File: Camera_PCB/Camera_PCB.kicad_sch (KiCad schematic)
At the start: 1 part, among them U1 V3s-eLQFP128

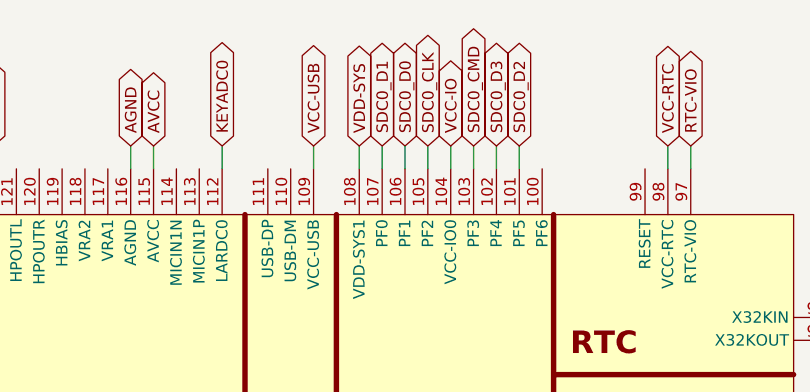
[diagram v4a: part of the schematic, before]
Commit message: Readded Camera, USB connections
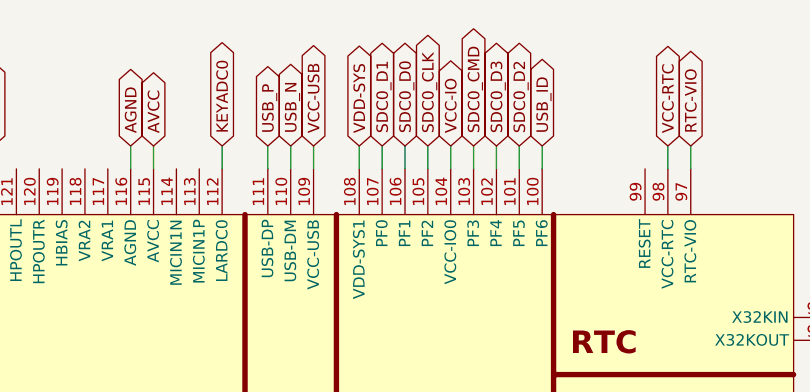
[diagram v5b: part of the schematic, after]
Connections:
- net USB_ID: now reaches U1.100 (PF6)
- net USB_N: now reaches U1.110 (USB-DM)
- net USB_P: now reaches U1.111 (USB-DP)
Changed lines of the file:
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@@
+	(wire
+		(pts
+			(xy 109.22 26.67) (xy 109.22 29.21)
+		)
+		(stroke
+			(width 0)
+			(type default)
+		)
+	)
 	(wire
 		(pts
@@
 	(wire
 		(pts
+			(xy 106.68 26.67) (xy 106.68 29.21)
+		)
+		(stroke
+			(width 0)
+			(type default)
+		)
+	)
+	(wire
+		(pts
 			(xy 170.18 95.25) (xy 172.72 95.25)
 		)
@@
 	(wire
 		(pts
+			(xy 137.16 26.67) (xy 137.16 29.21)
+		)
+		(stroke
+			(width 0)
+			(type default)
+		)
+	)
+	(wire
+		(pts
 			(xy 116.84 26.67) (xy 116.84 29.21)
 		)
@@
 		)
 	)
+	(global_label "USB_N"
+		(shape bidirectional)
+		(at 109.22 26.67 90)
+		(fields_autoplaced yes)
+		(effects
+			(font
+				(size 1.27 1.27)
+			)
+			(justify left)
+		)
+		(property "Intersheetrefs" "${INTERSHEET_REFS}"
+			(at 109.22 16.4654 90)
+			(effects
+				(font
+					(size 1.27 1.27)
+				)
+				(justify left)
+				(hide yes)
+			)
+		)
+	)
 	(global_label "VDD-CPU"
 		(shape bidirectional)
@@
 		)
 	)
+	(global_label "USB_P"
+		(shape bidirectional)
+		(at 106.68 26.67 90)
+		(fields_autoplaced yes)
+		(effects
+			(font
+				(size 1.27 1.27)
+			)
+			(justify left)
+		)
+		(property "Intersheetrefs" "${INTERSHEET_REFS}"
+			(at 106.68 16.5259 90)
+			(effects
+				(font
+					(size 1.27 1.27)
+				)
+				(justify left)
+				(hide yes)
+			)
+		)
+	)
 	(global_label "VDD-CPU"
 		(shape bidirectional)
@@
 		(property "Intersheetrefs" "${INTERSHEET_REFS}"
 			(at 187.0975 104.14 0)
+			(effects
+				(font
+					(size 1.27 1.27)
+				)
+				(justify left)
+				(hide yes)
+			)
+		)
+	)
+	(global_label "USB_ID"
+		(shape bidirectional)
+		(at 137.16 26.67 90)
+		(fields_autoplaced yes)
+		(effects
+			(font
+				(size 1.27 1.27)
+			)
+			(justify left)
+		)
+		(property "Intersheetrefs" "${INTERSHEET_REFS}"
+			(at 137.16 15.9211 90)
 			(effects
 				(font
@@
 	)
 	(sheet
+		(at 15.24 36.83)
+		(size 12.7 3.81)
+		(exclude_from_sim no)
+		(in_bom yes)
+		(on_board yes)
+		(dnp no)
+		(fields_autoplaced yes)
+		(stroke
+			(width 0.1524)
+			(type solid)
+		)
+		(fill
+			(color 0 0 0 0.0000)
+		)
+		(property "Sheetname" "Camera"
+			(at 15.24 36.1184 0)
+			(effects
+				(font
+					(size 1.27 1.27)
+				)
+				(justify left bottom)
+			)
+		)
+		(property "Sheetfile" "camera.kicad_sch"
+			(at 15.24 41.2246 0)
+			(effects
+				(font
+					(size 1.27 1.27)
+				)
+				(justify left top)
+			)
+		)
+		(instances
+			(project "Camera_PCB"
+				(path "/400c1603-202c-4359-a830-d2f0d06dd3ce"
+					(page "4")
+				)
+			)
+		)
+	)
+	(sheet
 		(at 15.24 16.51)
 		(size 12.7 3.81)
@@
 				)
 			)
-		)
-	)
-	(sheet
-		(at 15.24 36.83)
-		(size 12.7 3.81)
-		(exclude_from_sim no)
-		(in_bom yes)
-		(on_board yes)
-		(dnp no)
-		(fields_autoplaced yes)
-		(stroke
-			(width 0.1524)
-			(type solid)
-		)
-		(fill
-			(color 0 0 0 0.0000)
-		)
-		(property "Sheetname" "Camera"
-			(at 15.24 36.1184 0)
-			(effects
-				(font
-					(size 1.27 1.27)
-				)
-				(justify left bottom)
-			)
-		)
-		(property "Sheetfile" "camera.kicad_sch"
-			(at 15.24 41.2246 0)
-			(effects
-				(font
-					(size 1.27 1.27)
-				)
-				(justify left top)
-			)
-		)
-		(instances
-			(project "Camera_PCB"
-				(path "/400c1603-202c-4359-a830-d2f0d06dd3ce"
-					(page "4")
-				)
-			)

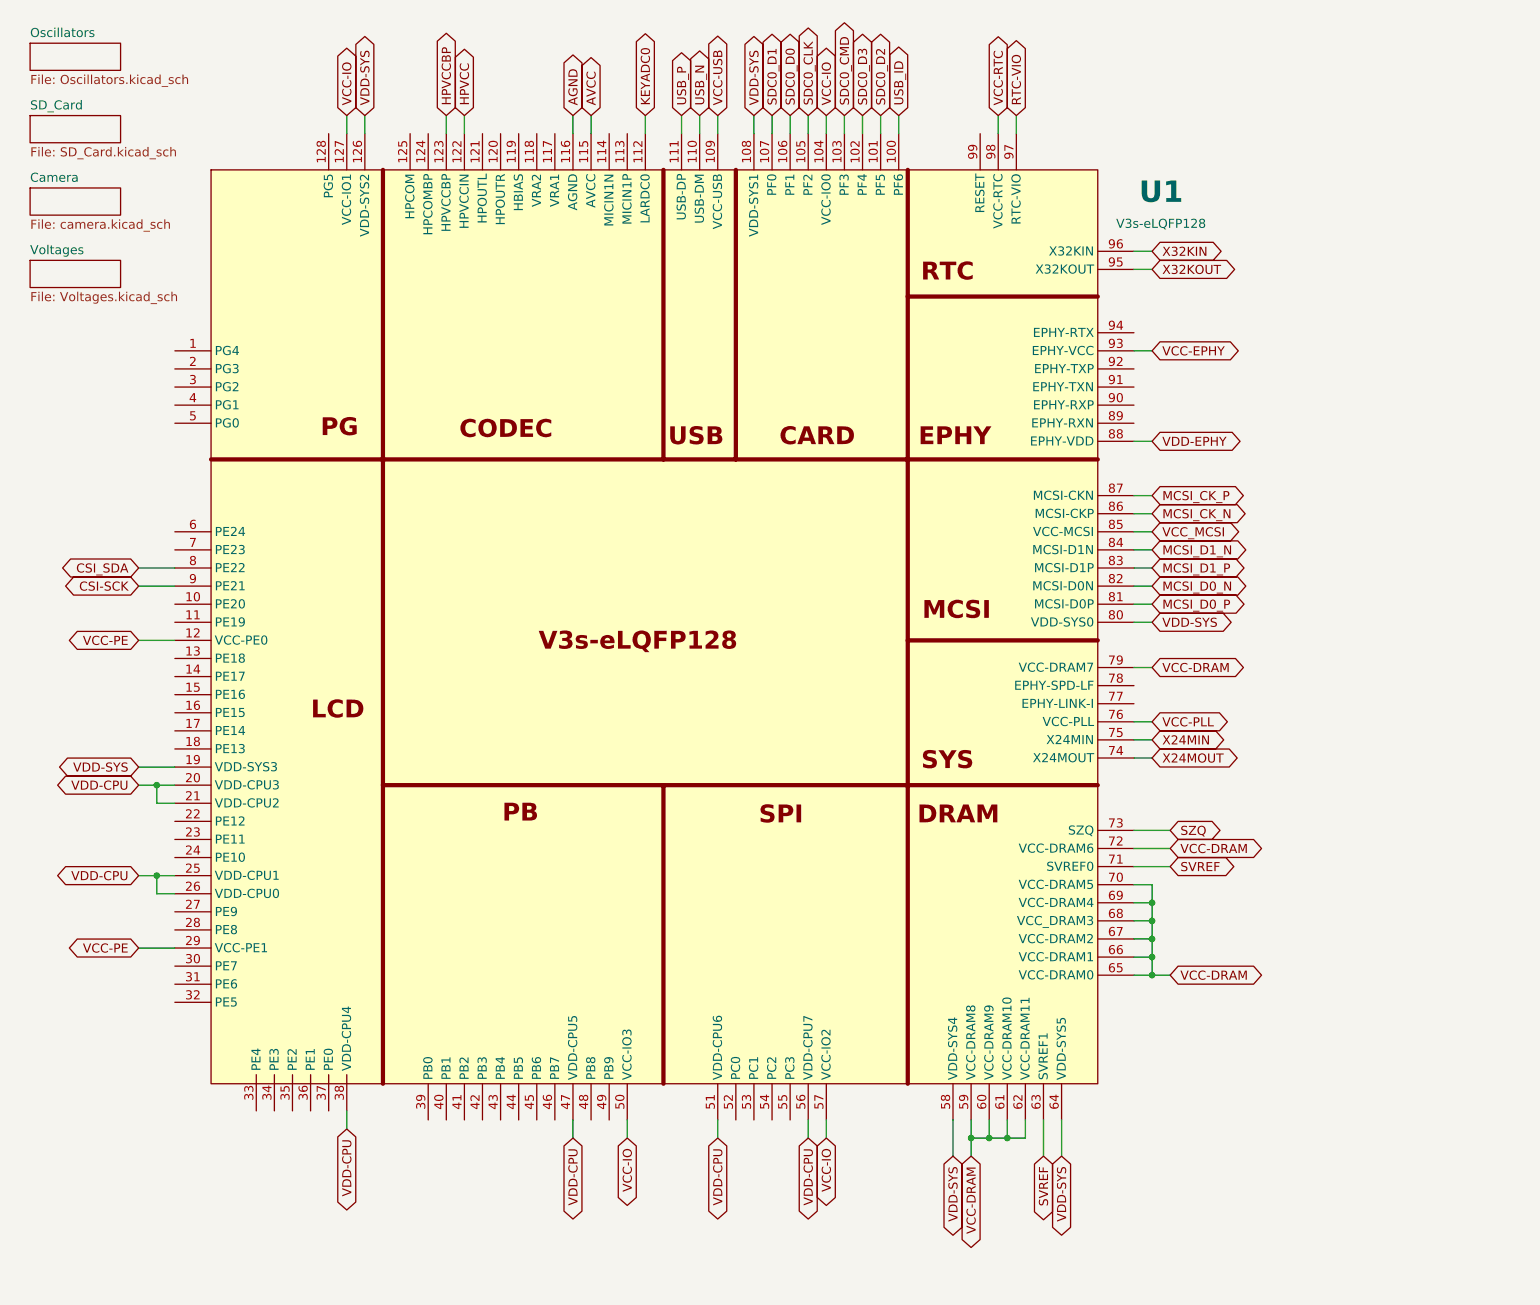
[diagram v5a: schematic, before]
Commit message: Added x pins + text
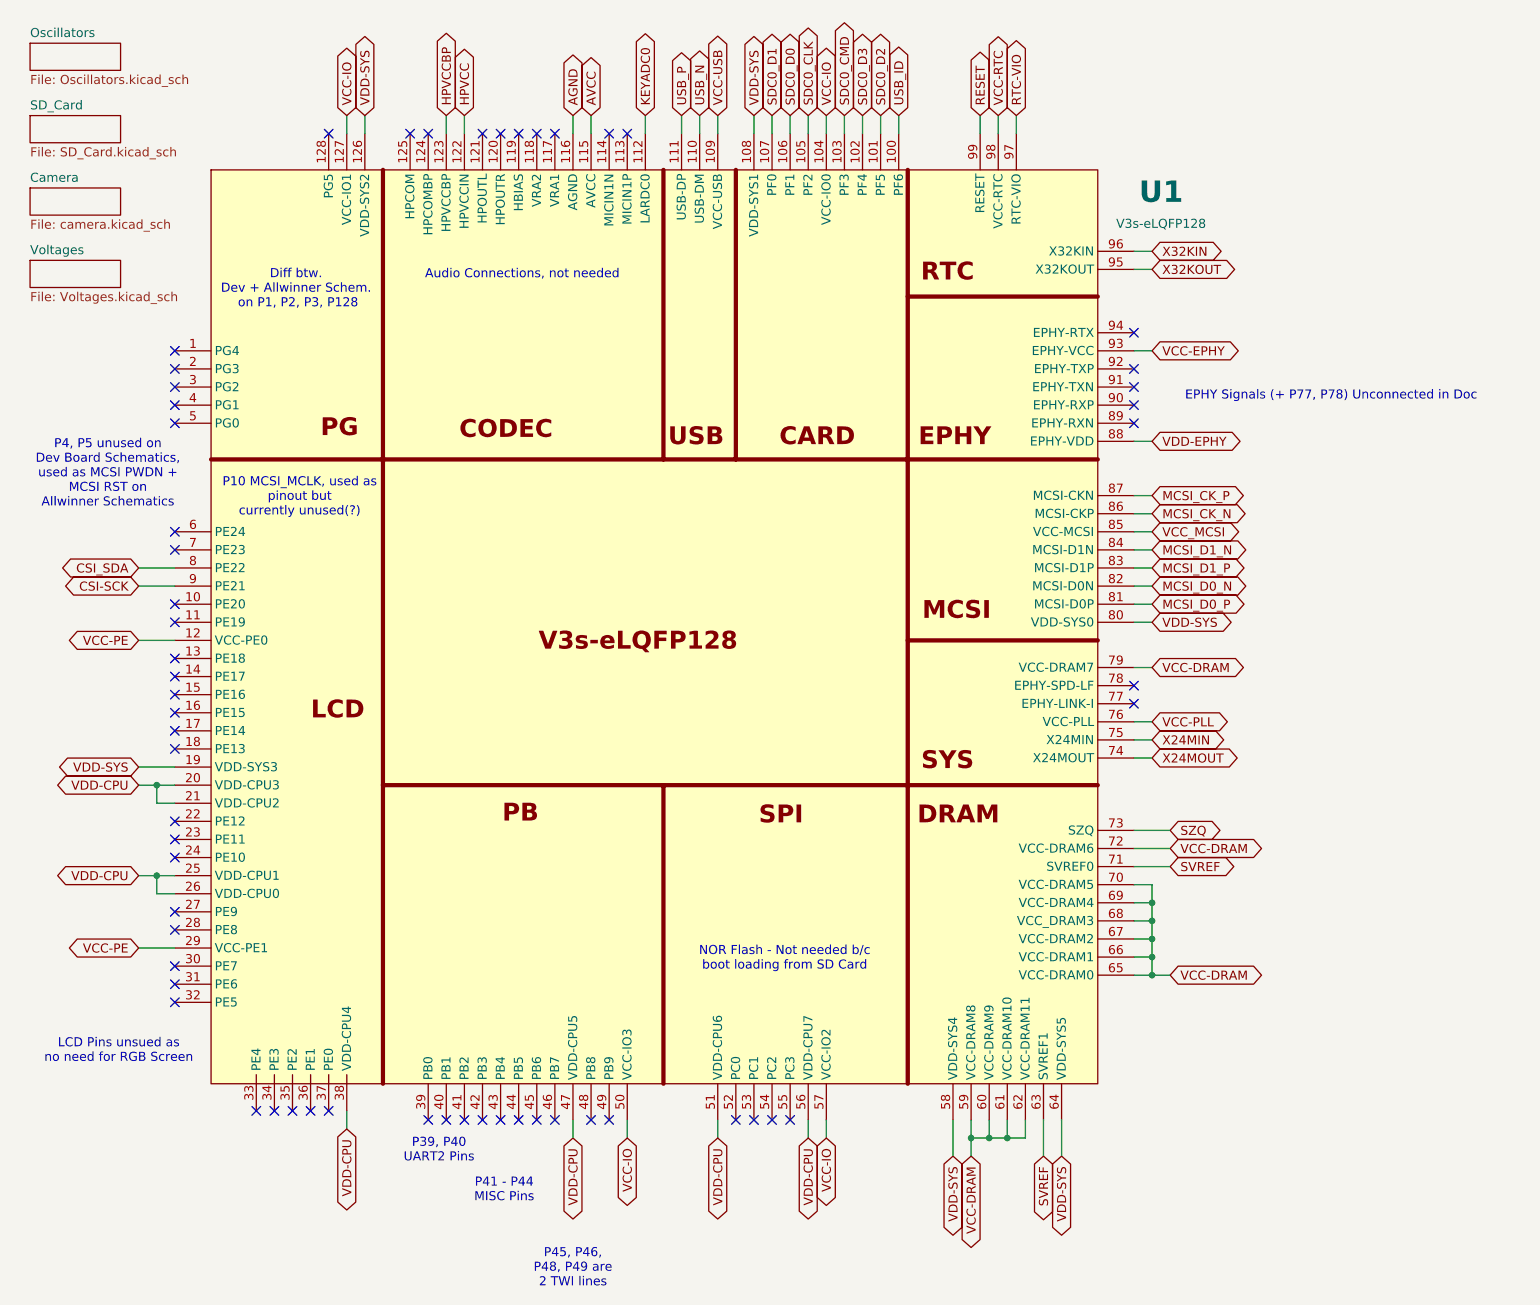
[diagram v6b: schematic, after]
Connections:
- net RESET: now reaches U1.99 (RESET)
- no-connect marks 0 -> 59
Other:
- note added: "Audio Connections, not needed"
- note added: "Diff btw. Dev + Allwinner Schem. on P1, P2, P3, P128"
- note added: "EPHY Signals (+ P77, P78) Unconnected in Doc"
- note added: "LCD Pins unsued as no need for RGB Screen"
- note added: "NOR Flash - Not needed b/c boot loading from SD Card"
- note added: "P10 MCSI_MCLK, used as pinout but currently unused(?)"
- note added: "P39, P40 UART2 Pins"
- note added: "P4, P5 unused on Dev Board Schematics, used as MCSI PWDN + MCSI RST on Allwinner Schematics"
- note added: "P41 - P44 MISC Pins"
- note added: "P45, P46, P48, P49 are 2 TWI lines"

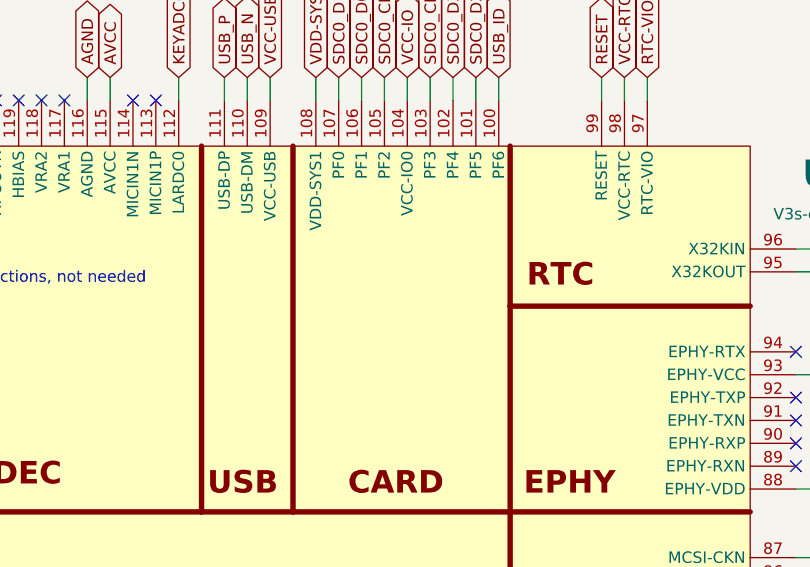
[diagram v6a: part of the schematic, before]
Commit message: Changed usb -> A 2.0
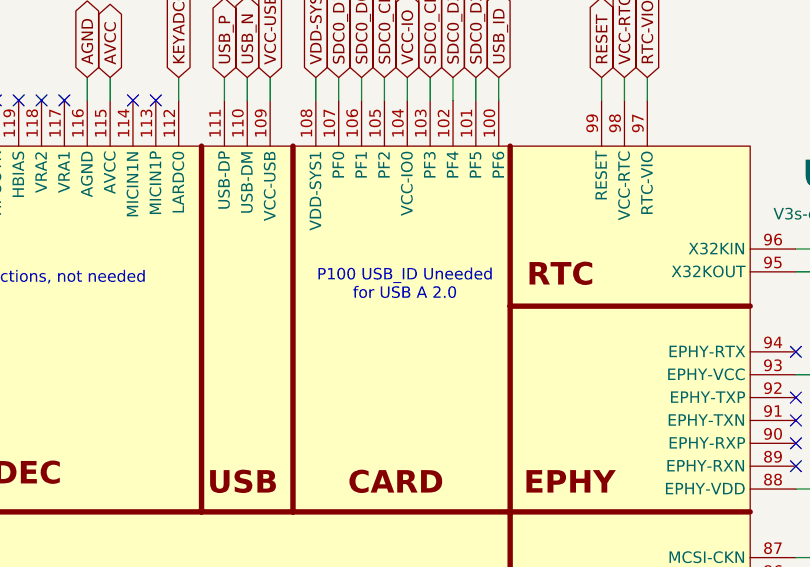
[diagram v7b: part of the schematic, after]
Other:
- note added: "P100 USB_ID Uneeded for USB A 2.0"
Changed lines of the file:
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@@
+		)
+	)
+	(text "P100 USB_ID Uneeded \nfor USB A 2.0"
+		(exclude_from_sim no)
+		(at 126.746 49.784 0)
+		(effects
+			(font
+				(size 1.27 1.27)
+			)
 		)
 	)

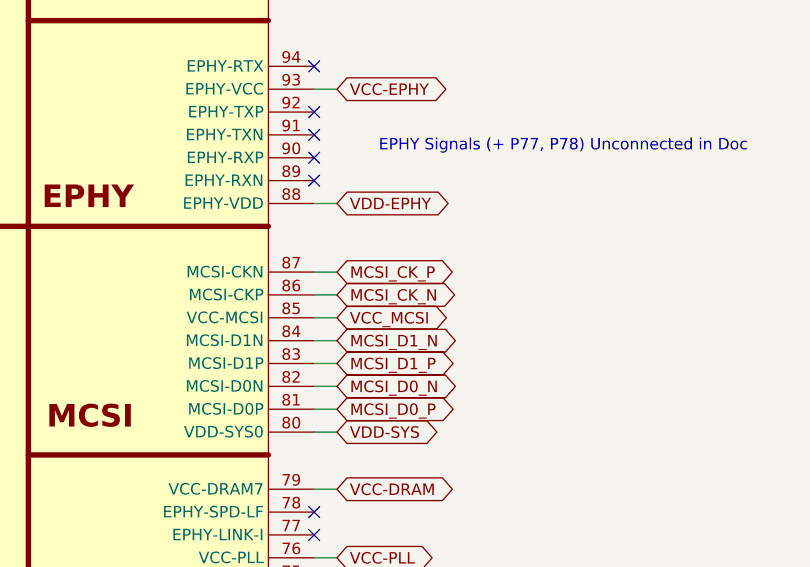
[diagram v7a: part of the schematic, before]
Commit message: Switched pins 86, 87
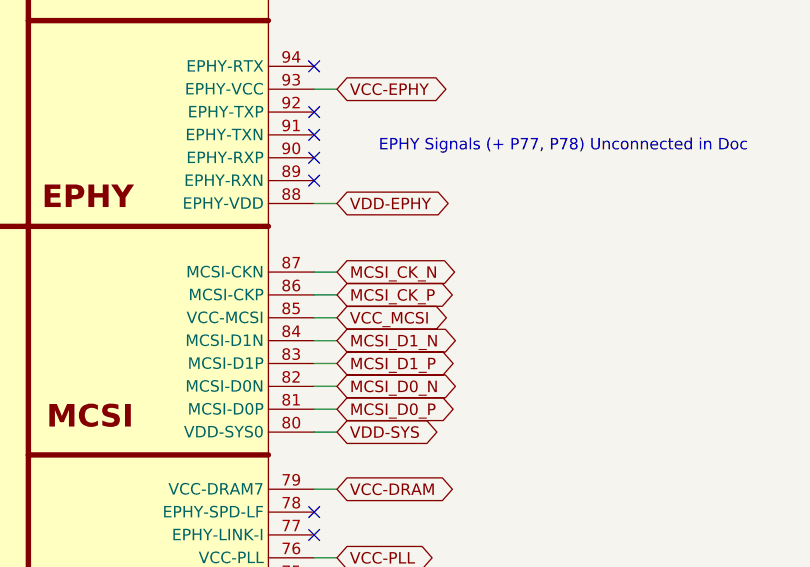
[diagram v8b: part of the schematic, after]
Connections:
- net MCSI_CK_N: now also U1.87 (MCSI-CKN); no longer U1.86 (MCSI-CKP)
- net MCSI_CK_P: now also U1.86 (MCSI-CKP); no longer U1.87 (MCSI-CKN)
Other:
- company: (none) -> Group 25 Senior Design
- title: (none) -> Wireless Backup Camera - Encoder
